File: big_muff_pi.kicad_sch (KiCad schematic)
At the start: 56 parts, among them Q1 BC817, Q2 BC817, Q3 BC817, Q5 BC817

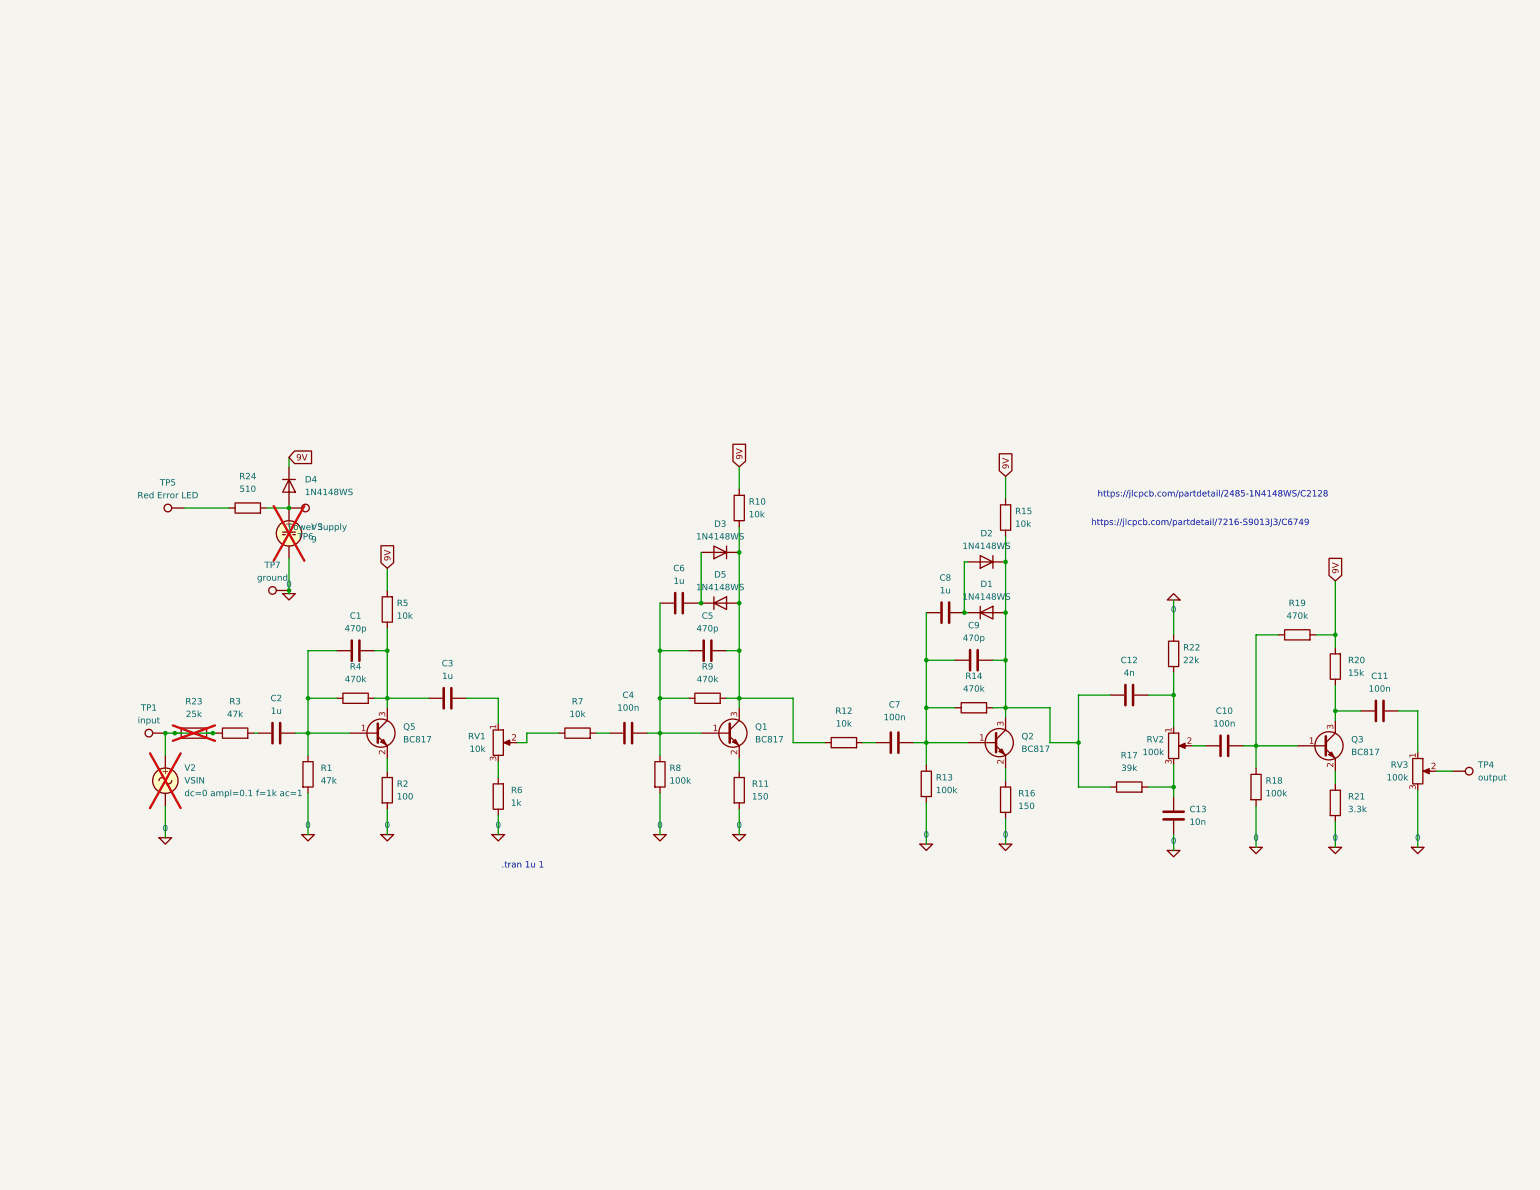
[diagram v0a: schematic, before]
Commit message: Moved to 0603, all basic parts. Placement done.
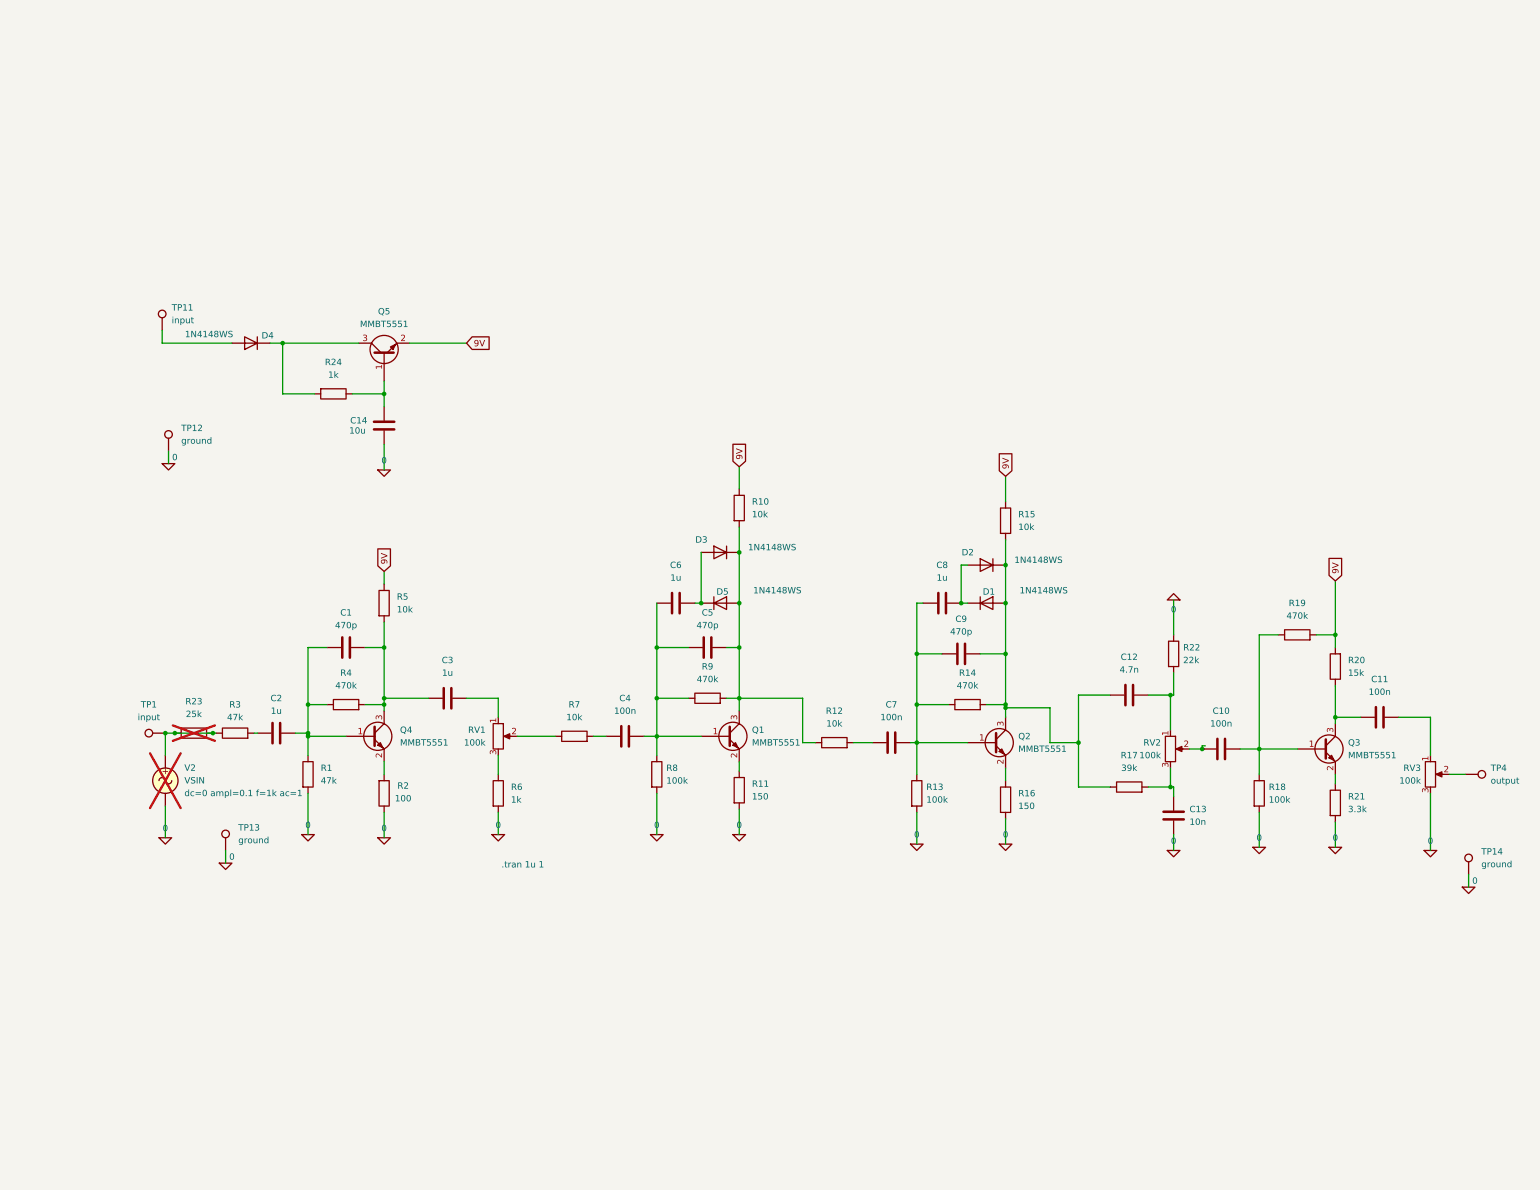
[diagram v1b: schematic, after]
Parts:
- removed TP5: Red Error LED, TestPoint:TestPoint_Pad_2.0x2.0mm, symbol Connector:TestPoint
- removed TP6: Power Supply, TestPoint:TestPoint_Pad_2.0x2.0mm, symbol Connector:TestPoint
- removed TP7: ground, TestPoint:TestPoint_Pad_2.0x2.0mm, symbol Connector:TestPoint
- removed V3: 9, symbol Simulation_SPICE:VDC
- added C14: 10u, Capacitor_SMD:C_0603_1608Metric_Pad1.08x0.95mm_HandSolder, symbol Device:C
- added Q4: MMBT5551, Package_TO_SOT_SMD:SOT-23, symbol Transistor_BJT:BC817
- added TP11: input, TestPoint:TestPoint_THTPad_2.5x2.5mm_Drill1.2mm, symbol Connector:TestPoint
- added TP12, TP13, TP14: ground, TestPoint:TestPoint_THTPad_2.5x2.5mm_Drill1.2mm, symbol Connector:TestPoint
- C1, C5, C9: footprint Capacitor_SMD:C_0402_1005Metric -> Capacitor_SMD:C_0603_1608Metric_Pad1.08x0.95mm_HandSolder; LCSC (none) -> C1620
- C10, C11, C4, C7: footprint Capacitor_SMD:C_0402_1005Metric -> Capacitor_SMD:C_0603_1608Metric_Pad1.08x0.95mm_HandSolder; LCSC (none) -> C14663
- C12: value 4n -> 4.7n; footprint Capacitor_SMD:C_0402_1005Metric -> Capacitor_SMD:C_0603_1608Metric_Pad1.08x0.95mm_HandSolder; LCSC (none) -> C53987
- C13: footprint Capacitor_SMD:C_0402_1005Metric -> Capacitor_SMD:C_0603_1608Metric_Pad1.08x0.95mm_HandSolder; LCSC (none) -> C57112
- C2, C3, C6, C8: footprint Capacitor_SMD:C_0402_1005Metric -> Capacitor_SMD:C_0603_1608Metric_Pad1.08x0.95mm_HandSolder; LCSC (none) -> C15849
- D1, D2, D3, D4, D5: LCSC (none) -> C2128
- Q1, Q2, Q3, Q5: value BC817 -> MMBT5551; LCSC (none) -> C2145
- R1, R3: footprint Resistor_SMD:R_0402_1005Metric -> Resistor_SMD:R_0603_1608Metric_Pad0.98x0.95mm_HandSolder; LCSC (none) -> C25819
- R10, R12, R15, R5, R7: footprint Resistor_SMD:R_0402_1005Metric -> Resistor_SMD:R_0603_1608Metric_Pad0.98x0.95mm_HandSolder; LCSC (none) -> C25804
- R11, R16: footprint Resistor_SMD:R_0402_1005Metric -> Resistor_SMD:R_0603_1608Metric_Pad0.98x0.95mm_HandSolder; LCSC (none) -> C22808
- R13, R18, R8: footprint Resistor_SMD:R_0402_1005Metric -> Resistor_SMD:R_0603_1608Metric_Pad0.98x0.95mm_HandSolder; LCSC (none) -> C25803
- R14, R19, R4, R9: footprint Resistor_SMD:R_0402_1005Metric -> Resistor_SMD:R_0603_1608Metric_Pad0.98x0.95mm_HandSolder; LCSC (none) -> C23178
- R17: footprint Resistor_SMD:R_0402_1005Metric -> Resistor_SMD:R_0603_1608Metric_Pad0.98x0.95mm_HandSolder; LCSC (none) -> C23153
- R2: footprint Resistor_SMD:R_0402_1005Metric -> Resistor_SMD:R_0603_1608Metric_Pad0.98x0.95mm_HandSolder; LCSC (none) -> C22775
- R20: footprint Resistor_SMD:R_0402_1005Metric -> Resistor_SMD:R_0603_1608Metric_Pad0.98x0.95mm_HandSolder; LCSC (none) -> C22809
- R21: footprint Resistor_SMD:R_0402_1005Metric -> Resistor_SMD:R_0603_1608Metric_Pad0.98x0.95mm_HandSolder; LCSC (none) -> C22978
- R22: footprint Resistor_SMD:R_0402_1005Metric -> Resistor_SMD:R_0603_1608Metric_Pad0.98x0.95mm_HandSolder; LCSC (none) -> C31850
- R24: value 510 -> 1k; footprint Resistor_SMD:R_0402_1005Metric -> Resistor_SMD:R_0603_1608Metric_Pad0.98x0.95mm_HandSolder; LCSC (none) -> C21190
- R6: footprint Resistor_SMD:R_0402_1005Metric -> Resistor_SMD:R_0603_1608Metric_Pad0.98x0.95mm_HandSolder; LCSC (none) -> C21190
- RV1: value 10k -> 100k
- TP1, TP4: footprint TestPoint:TestPoint_Pad_2.0x2.0mm -> TestPoint:TestPoint_THTPad_2.5x2.5mm_Drill1.2mm
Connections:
- net 0: now also R2.1, R6.2, C14.2, TP12.1, TP13.1, TP14.1; no longer R2.2, R6.1
- net 9V: now also Q5.2 (E), R10.1, R15.1, R5.1; no longer D4.1 (K), R10.2, R15.2, R5.2
- net at C5.2, D3.1 (K), D5.2 (A)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: now also R10.2; no longer R10.1
- net at C1.2, C3.1, R4.2: now also R5.2, Q4.3 (C); no longer Q5.3 (C), R5.1
- net at C12.1, C9.2, D1.2 (A)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: now also R15.2; no longer R15.1
- net at C1.1, C2.2, R1.1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: now also Q4.1 (B); no longer Q5.1 (B)
- net at RV1.3: now also R6.1; no longer R6.2
- net at R24.2: now also D4.1 (K), Q5.3 (C); no longer D4.2 (A)
- net at R24.1: now also Q5.1 (B), C14.1
- new net: D4.2 (A), TP11.1
- new net: Q4.2 (E), R2.2
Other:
- note removed: "https://jlcpcb.com/partdetail/2485-1N4148WS/C2128"
- note removed: "https://jlcpcb.com/partdetail/7216-S9013J3/C6749"
- moved on the sheet: C1, RV1, RV2, RV3, TP4

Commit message: Added capacitance, switches.
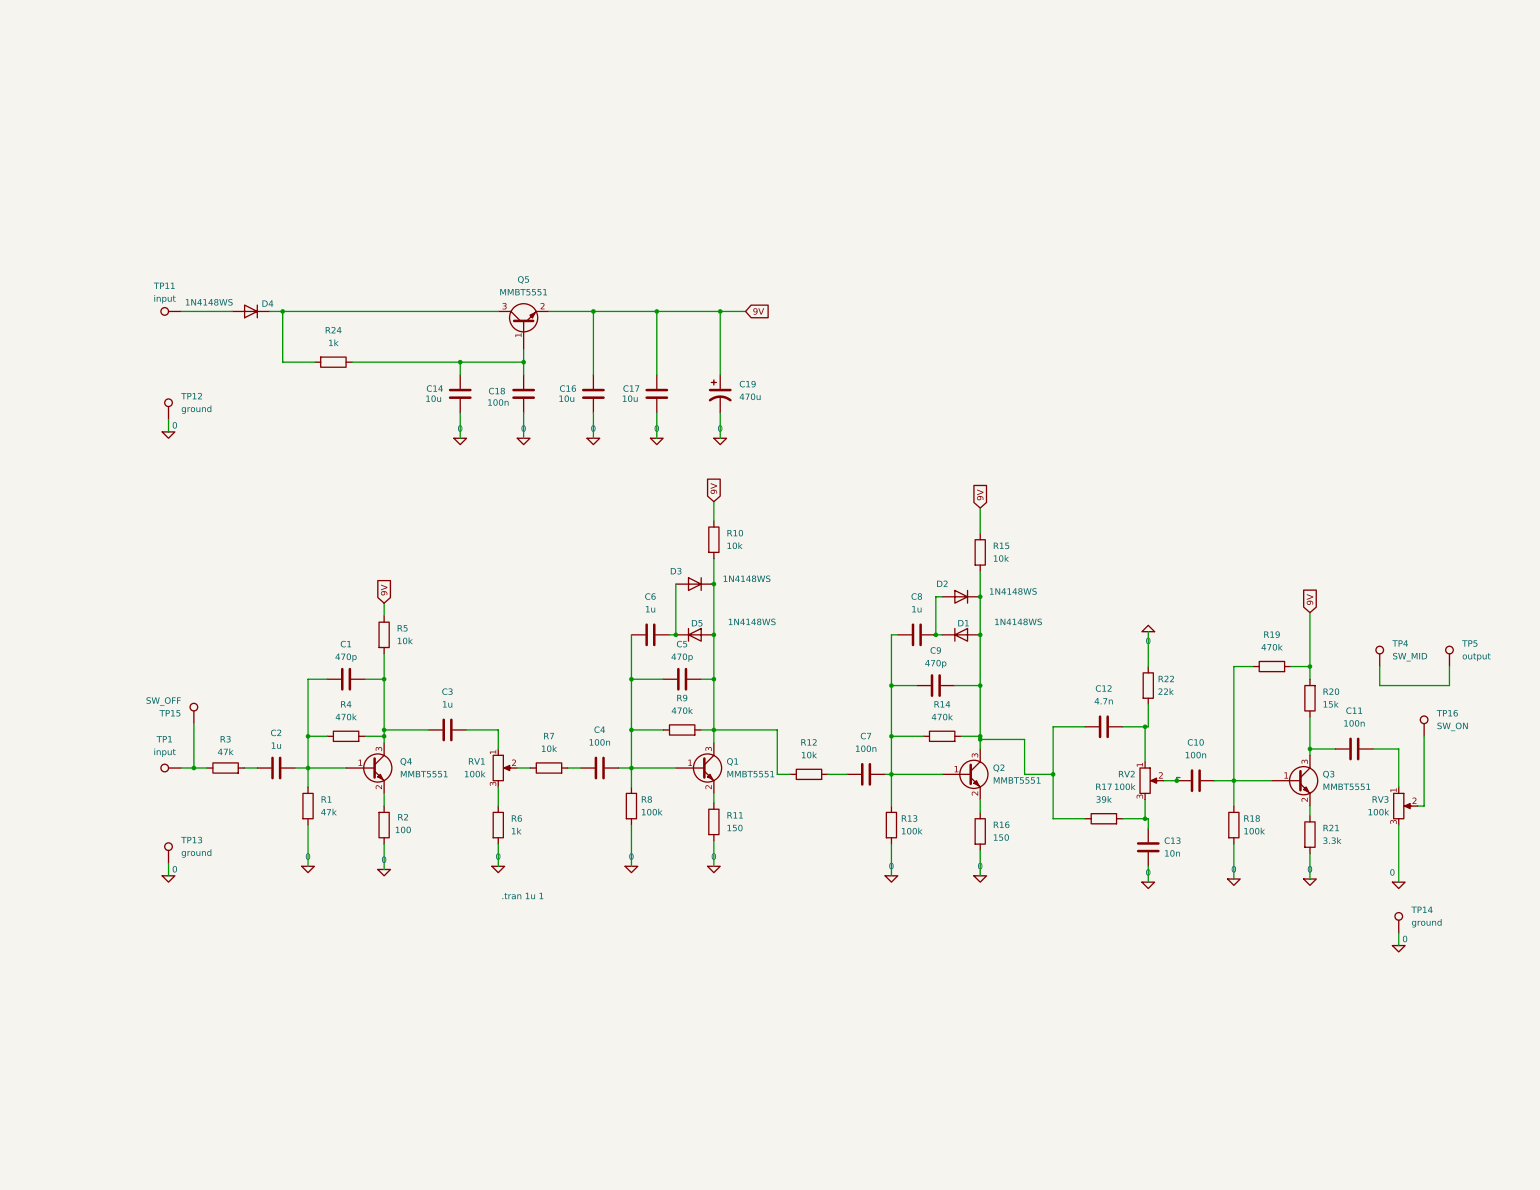
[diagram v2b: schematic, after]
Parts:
- removed R23: 25k, Resistor_SMD:R_0402_1005Metric, symbol Device:R
- removed V2: VSIN, symbol Simulation_SPICE:VSIN
- added C16, C17: 10u, Capacitor_SMD:C_0603_1608Metric_Pad1.08x0.95mm_HandSolder, symbol Device:C
- added C18: 100n, Capacitor_SMD:C_0603_1608Metric_Pad1.08x0.95mm_HandSolder, symbol Device:C
- added C19: 470u, Capacitor_THT:CP_Radial_D8.0mm_P3.50mm, symbol Device:C_Polarized_US
- added TP15: SW_OFF, TestPoint:TestPoint_THTPad_2.5x2.5mm_Drill1.2mm, symbol Connector:TestPoint
- added TP16: SW_ON, TestPoint:TestPoint_THTPad_2.5x2.5mm_Drill1.2mm, symbol Connector:TestPoint
- added TP5: output, TestPoint:TestPoint_THTPad_2.5x2.5mm_Drill1.2mm, symbol Connector:TestPoint
- TP4: value output -> SW_MID
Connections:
- net 0: now also C16.2, C17.2, C18.1, C19.2
- net 9V: now also C16.1, C17.1, C19.1
- net at R3.1, TP1.1: now also TP15.1
- net at TP4.1: now also TP5.1; no longer RV3.2
- net at C14.1, Q5.1 (B), R24.1: now also C18.2
- new net: RV3.2, TP16.1
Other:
- moved on the sheet: C1, C10, C11, C12, C13, C14, C2, C3, C4, C5, C6, C7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

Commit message: Added connectors and switched.
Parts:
- removed TP1: input, TestPoint:TestPoint_THTPad_2.5x2.5mm_Drill1.2mm, symbol Connector:TestPoint
- removed TP13: ground, TestPoint:TestPoint_THTPad_2.5x2.5mm_Drill1.2mm, symbol Connector:TestPoint
- removed TP5: output, TestPoint:TestPoint_THTPad_2.5x2.5mm_Drill1.2mm, symbol Connector:TestPoint
- added J1, J2: NMJ6HHD2, Connector_Audio:Jack_6.35mm_Neutrik_NMJ6HHD2_Horizontal, symbol Connector_Audio:NMJ6HHD2
- added SW1: SW_DPDT_x2, switch:switch_DPDT, symbol Switch:SW_DPDT_x2
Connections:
- net 0: now also J1.R, J2.R
- net at R3.1, TP15.1: now also J1.T
- net at TP4.1: now also J2.T
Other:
- moved on the sheet: C1, C2, C3, Q4, R1, R2, R3, R4, R5, R6, R7, RV1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
